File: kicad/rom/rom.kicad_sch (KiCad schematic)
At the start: 4 parts, among them J1 Board Connector, U1 28C256

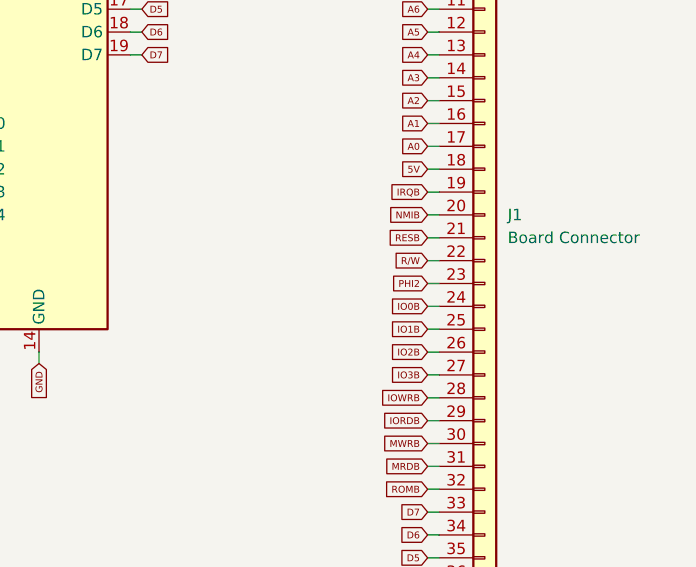
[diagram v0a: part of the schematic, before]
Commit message: integrated wozmon, updated kicad to specify phi1o
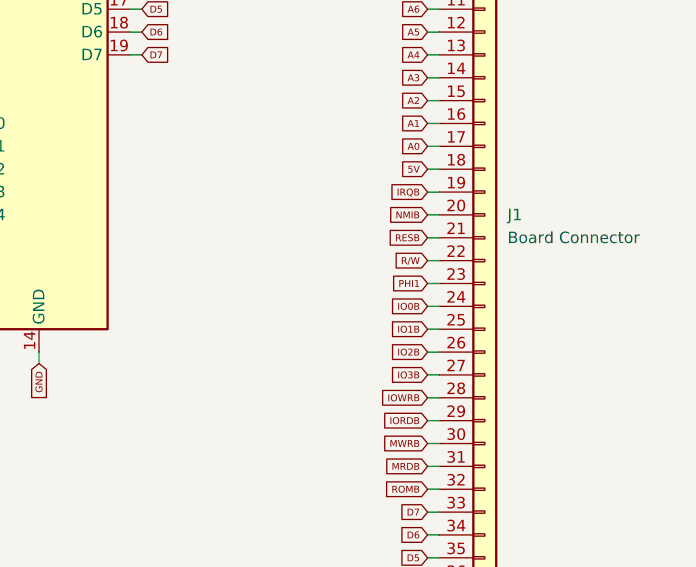
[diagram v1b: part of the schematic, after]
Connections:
- net PHI2 renamed PHI1
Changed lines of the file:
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@@
 		)
 	)
-	(global_label "PHI2"
+	(global_label "PHI1"
 		(shape input)
 		(at 217.17 102.87 180)
